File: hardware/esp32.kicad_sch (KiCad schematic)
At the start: 6 parts, among them SW1 SW_Push, U2 ESP32-S3-WROOM-1

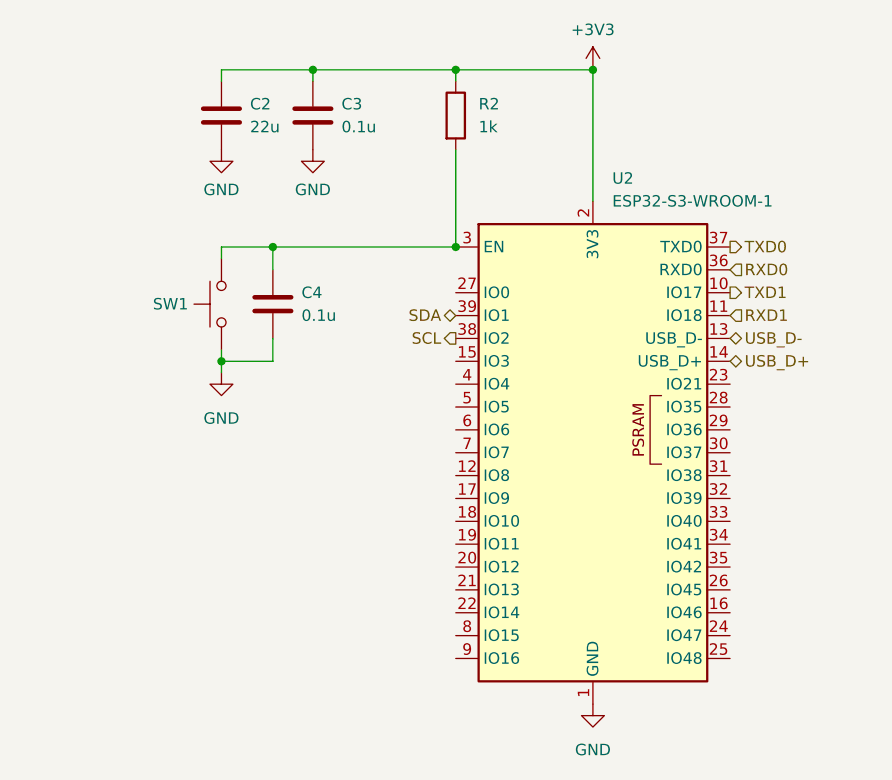
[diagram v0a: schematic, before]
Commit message: new symbol + some buses
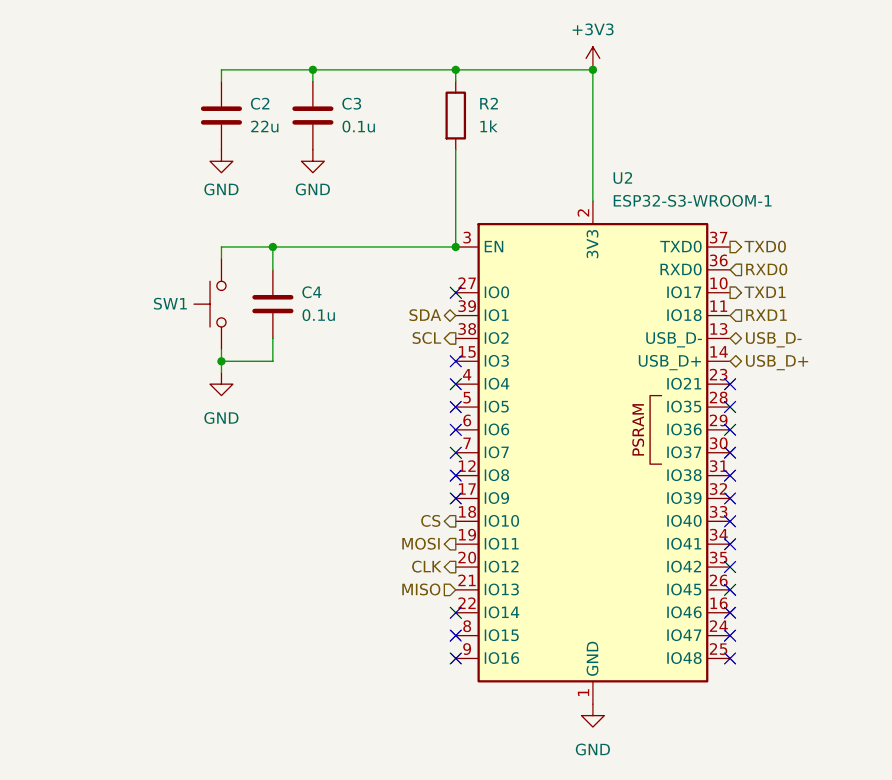
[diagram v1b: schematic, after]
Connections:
- net CS: now reaches U2.18 (IO10)
- net MOSI: now reaches U2.19 (IO11)
- net CLK: now reaches U2.20 (IO12)
- net MISO: now reaches U2.21 (IO13)
- no-connect marks 0 -> 24
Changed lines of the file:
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@@
 		(color 0 0 0 0)
+	)
+	(no_connect
+		(at 106.68 109.22)
+	)
+	(no_connect
+		(at 106.68 76.2)
+	)
+	(no_connect
+		(at 106.68 81.28)
+	)
+	(no_connect
+		(at 137.16 81.28)
+	)
+	(no_connect
+		(at 106.68 91.44)
+	)
+	(no_connect
+		(at 137.16 91.44)
+	)
+	(no_connect
+		(at 137.16 88.9)
+	)
+	(no_connect
+		(at 137.16 78.74)
+	)
+	(no_connect
+		(at 137.16 104.14)
+	)
+	(no_connect
+		(at 137.16 86.36)
+	)
+	(no_connect
+		(at 137.16 109.22)
+	)
+	(no_connect
+		(at 137.16 106.68)
+	)
+	(no_connect
+		(at 106.68 86.36)
+	)
+	(no_connect
+		(at 106.68 88.9)
+	)
+	(no_connect
+		(at 106.68 106.68)
+	)
+	(no_connect
+		(at 106.68 104.14)
+	)
+	(no_connect
+		(at 106.68 78.74)
+	)
+	(no_connect
+		(at 106.68 83.82)
+	)
+	(no_connect
+		(at 137.16 93.98)
+	)
+	(no_connect
+		(at 137.16 96.52)
+	)
+	(no_connect
+		(at 137.16 99.06)
+	)
+	(no_connect
+		(at 137.16 83.82)
+	)
+	(no_connect
+		(at 137.16 101.6)
+	)
+	(no_connect
+		(at 106.68 68.58)
 	)
 	(wire
@@
 		)
 	)
+	(hierarchical_label "MISO"
+		(shape input)
+		(at 106.68 101.6 180)
+		(effects
+			(font
+				(size 1.27 1.27)
+			)
+			(justify right)
+		)
+	)
 	(hierarchical_label "RXD1"
 		(shape input)
@@
 		)
 	)
+	(hierarchical_label "CLK"
+		(shape output)
+		(at 106.68 99.06 180)
+		(effects
+			(font
+				(size 1.27 1.27)
+			)
+			(justify right)
+		)
+	)
 	(hierarchical_label "SCL"
 		(shape output)
@@
 		)
 	)
+	(hierarchical_label "CS"
+		(shape output)
+		(at 106.68 93.98 180)
+		(effects
+			(font
+				(size 1.27 1.27)
+			)
+			(justify right)
+		)
+	)
+	(hierarchical_label "MOSI"
+		(shape output)
+		(at 106.68 96.52 180)
+		(effects
+			(font
+				(size 1.27 1.27)
+			)
+			(justify right)
+		)
+	)

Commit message: drew more busses and connections
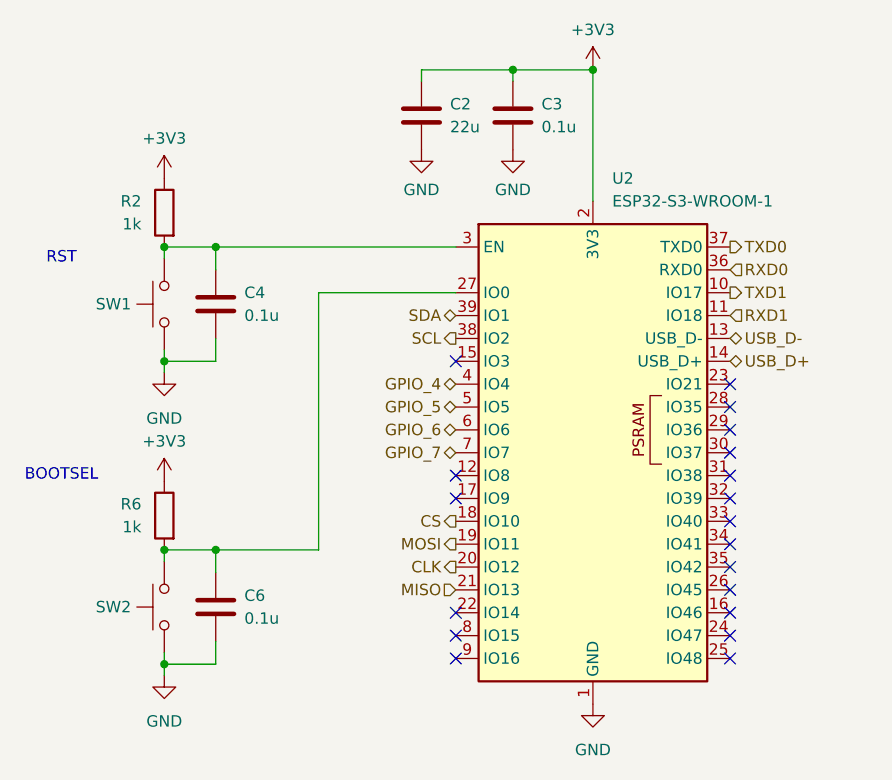
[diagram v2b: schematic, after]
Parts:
- added C6: 0.1u, symbol Device:C
- added R6: 1k, symbol Device:R
- added SW2: SW_Push, symbol Switch:SW_Push
- U2: Datasheet 2 (none) -> https://documentation.espressif.com/esp32-s3_datasheet_en.p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
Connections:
- net +3V3: now also R6.1
- net GND: now also C6.2, SW2.1
- net at U2.27 (IO0): now also C6.1, R6.2, SW2.2
- net GPIO_4: now reaches U2.4 (IO4)
- net GPIO_5: now reaches U2.5 (IO5)
- net GPIO_6: now reaches U2.6 (IO6)
- net GPIO_7: now reaches U2.7 (IO7)
- no-connect marks 24 -> 19
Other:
- note added: "BOOTSEL"
- note added: "RST"
- moved on the sheet: C2, C3, C4, R2, SW1

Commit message: beginnings of power distribution maybe?
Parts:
- U2: value ESP32-S3-WROOM-1 -> ESP32-S3-WROOM-1-N16
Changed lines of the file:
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@@
+		)
+	)
+	(table
+		(column_count 2)
+		(border
+			(external yes)
+			(header yes)
+			(stroke
+				(width 0)
+				(type solid)
+			)
+		)
+		(separators
+			(rows yes)
+			(cols yes)
+			(stroke
+				(width 0)
+				(type solid)
+			)
+		)
+		(column_widths 21.59 19.685)
+		(row_heights 3.81)
+		(cells
+			(table_cell "Recommended I_{VCC}"
+				(exclude_from_sim no)
+				(at 165.735 67.31 0)
+				(size 21.59 3.81)
+				(margins 0.9525 0.9525 0.9525 0.9525)
+				(span 1 1)
+				(fill
+					(type none)
+				)
+				(effects
+					(font
+						(size 1.27 1.27)
+					)
+					(justify left top)
+				)
+			)
+			(table_cell "500 mA"
+				(exclude_from_sim no)
+				(at 187.325 67.31 0)
+				(size 19.685 3.81)
+				(margins 0.9525 0.9525 0.9525 0.9525)
+				(span 1 1)
+				(fill
+					(type none)
+				)
+				(effects
+					(font
+						(size 1.27 1.27)
+					)
+					(justify left top)
+				)
+			)
 		)
 	)
@@
 			)
 		)
-		(property "Value" "ESP32-S3-WROOM-1"
+		(property "Value" "ESP32-S3-WROOM-1-N16"
 			(at 124.0633 58.42 0)
 			(effects
